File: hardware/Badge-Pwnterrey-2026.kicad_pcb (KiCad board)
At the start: 2 copper layers, 23 parts, among them P1 USB_C_Plug_USB2.0, SW1 RESET, SW2 GPIO, U1 ESP32-C5-WROOM-1-N4, U2 AP2112K-3.3, U3 NT3H2111W0FHK

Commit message: feat(Hw):Init_Floorplan
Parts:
- added SW3: On, Footprints:MSK12C02, F.Cu at (187.8, 82.0)
- moved C1 188.1 mm to (238.4, 65.2), turned to 0 degrees
- moved C3 186.7 mm to (238.4, 66.7), turned to 0 degrees
- moved U1 170.4 mm to (233.2, 78.3), turned to -90 degrees
- moved C4 131.5 mm to (231.9, 58.3)
- moved R1 131.5 mm to (234.8, 58.3)
- moved SW1 131.5 mm to (233.3, 54.5)
- moved F1 124.0 mm to (197.2, 67.1)
- moved R3 124.0 mm to (197.1, 62.6)
- moved R4 124.0 mm to (197.2, 65.6)
- moved P1 124.0 mm to (192.7, 63.9)
- moved R2 101.7 mm to (224.7, 58.4)
- moved C5 101.7 mm to (221.7, 58.4)
- moved SW2 101.7 mm to (223.2, 54.5)
- moved C9 101.0 mm to (199.9, 82.8), turned to 0 degrees
- moved U2 98.3 mm to (199.8, 79.5), turned to 90 degrees
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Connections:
- C9 pad 1: VBUS -> Net-(SW3A-B)
- U2 pad 1: VBUS -> Net-(SW3A-B)
- U2 pad 3: VBUS -> Net-(SW3A-B)
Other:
- board outline added: 54 x 85.6 mm

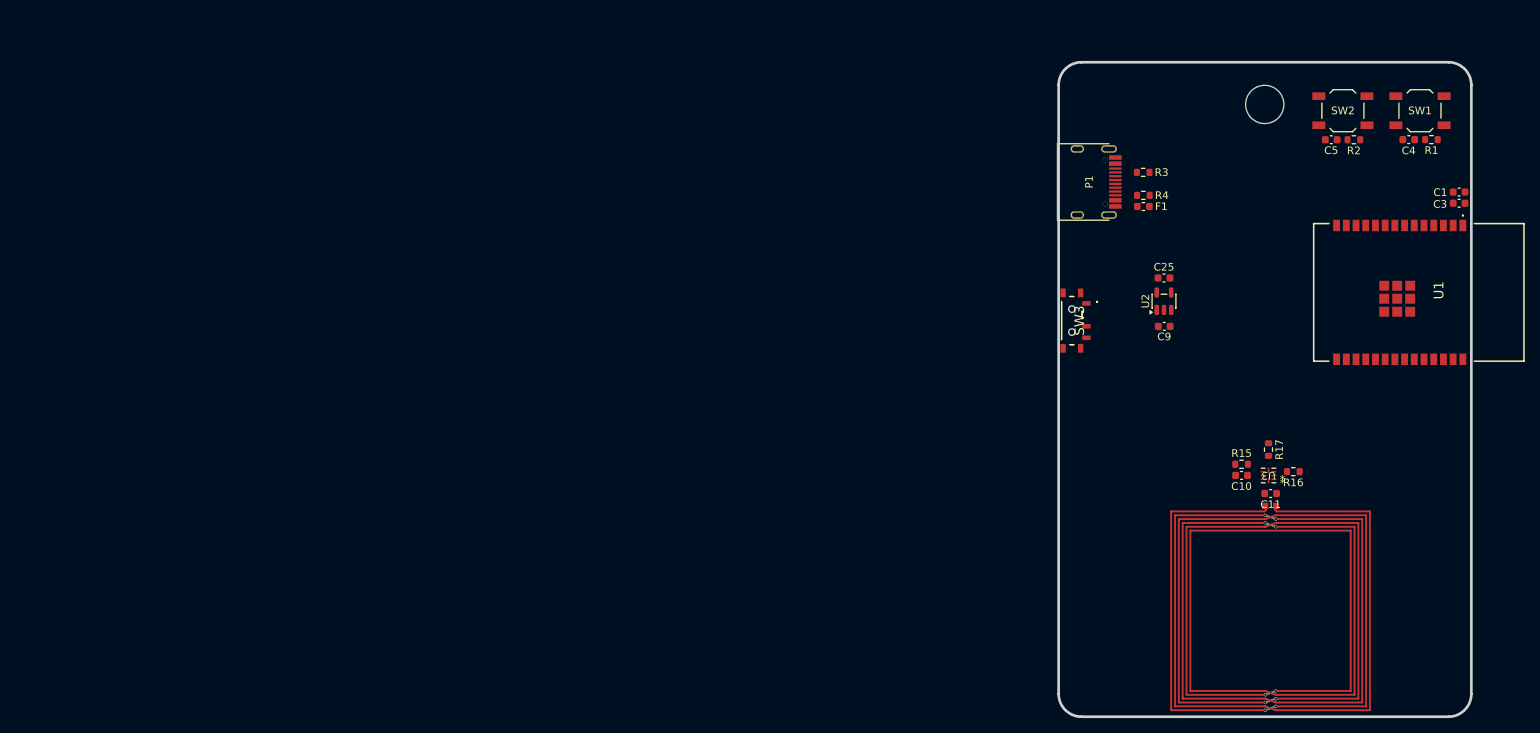
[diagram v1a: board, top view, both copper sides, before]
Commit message: feat(Hw):Update_Schematic_And_Init_Route
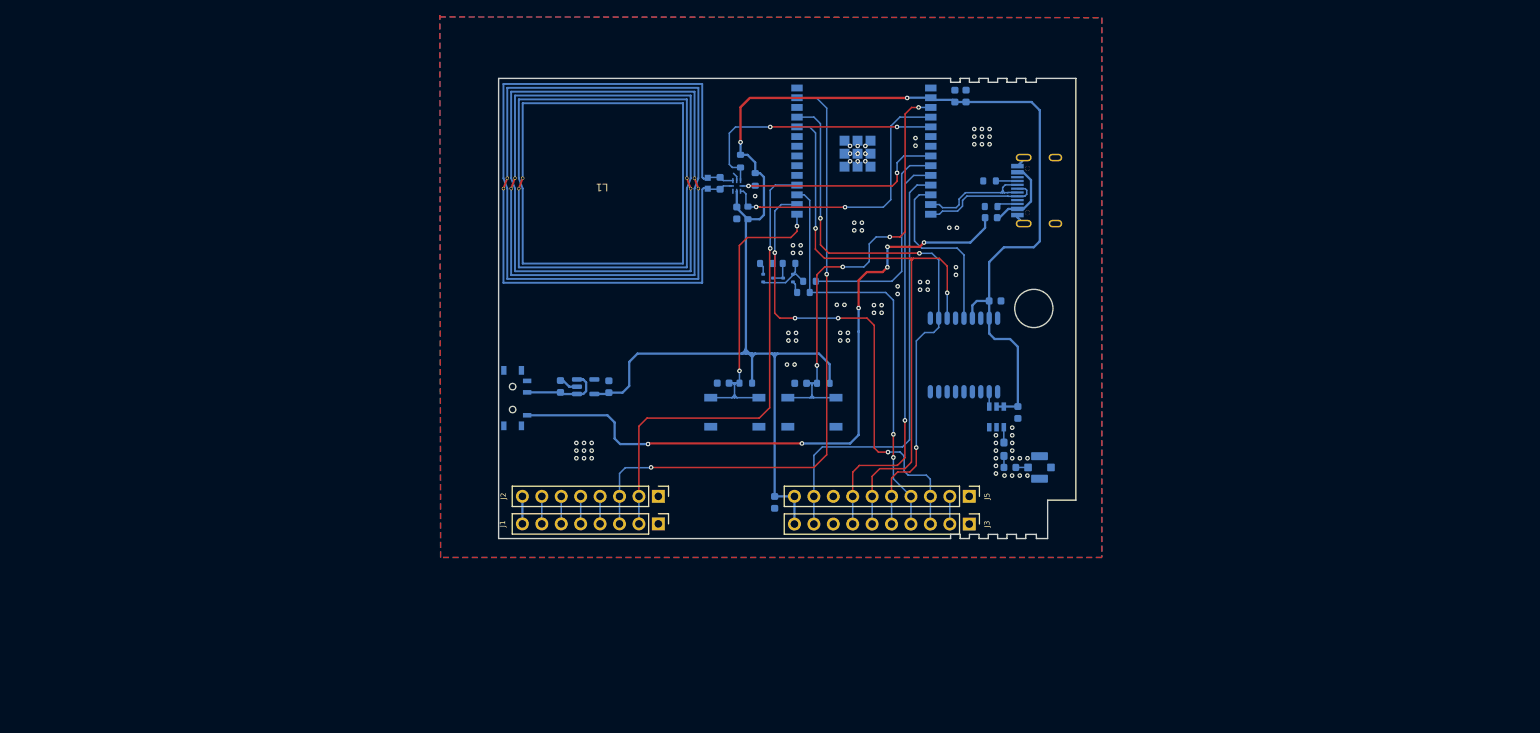
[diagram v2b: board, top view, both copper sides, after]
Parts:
- added AE1: Antenna_Shield, Connector_Coaxial:U.FL_Molex_MCRF_73412-0110_Vertical, B.Cu at (183.6, 101.2)
- added C14: 10uF, Capacitor_SMD:C_0603_1608Metric, B.Cu at (177.8, 79.4)
- added C15: 0.1uF, Capacitor_SMD:C_0603_1608Metric, B.Cu at (180.7, 94.0)
- added C2: 10uF, Capacitor_SMD:C_0603_1608Metric, B.Cu at (148.9, 105.8)
- added C6: 470pF, Capacitor_SMD:C_0603_1608Metric, B.Cu at (179.7, 101.2)
- added J1: Conn_01x08_Socket, Connector_PinHeader_2.54mm:PinHeader_1x08_P2.54mm_Vertical, F.Cu at (133.7, 108.6)
- added J2: Conn_01x08_Socket, Connector_PinHeader_2.54mm:PinHeader_1x08_P2.54mm_Vertical, F.Cu at (133.7, 105.0)
- added J3: Conn_01x10_Socket, Connector_PinHeader_2.54mm:PinHeader_1x10_P2.54mm_Vertical, F.Cu at (174.4, 108.6)
- added J5: Conn_01x10_Socket, Connector_PinHeader_2.54mm:PinHeader_1x10_P2.54mm_Vertical, F.Cu at (174.4, 105.0)
- added L2: 6.8nH, Inductor_SMD:L_0603_1608Metric_Pad1.05x0.95mm_HandSolder, B.Cu at (178.9, 98.8)
- added Q1: DMP2004TK-7, Package_TO_SOT_SMD:SOT-523, B.Cu at (148.1, 76.4)
- added Q2: DMP2004TK-7, Package_TO_SOT_SMD:SOT-523, B.Cu at (150.7, 76.4)
- added R6: 150, Resistor_SMD:R_0603_1608Metric, B.Cu at (153.5, 76.9)
- added R7: 10K, Resistor_SMD:R_0603_1608Metric, B.Cu at (150.8, 74.5)
- added R8: 4k7, Resistor_SMD:R_0603_1608Metric, B.Cu at (147.8, 74.5)
- added R9: 4k7, Resistor_SMD:R_0603_1608Metric, B.Cu at (152.7, 78.3)
- added U4: LNA, Footprints:AT2659S-LSA, B.Cu at (177.9, 94.6)
- added U5: GPS, Footprints:GPSM-SMD_ATGM336H, B.Cu at (173.7, 86.5)
- C1, C10, C11, C25, C3, C4, C5, C9, F1, P1, R1, R15, R16, R17, R2, R3, R4, SW1, SW2, SW3, U1, U2, U3: moved to B.Cu
- L1: moved to F.Cu
- moved L1 103.8 mm to (126.3, 64.1), turned to 180 degrees
- moved SW1 88.8 mm to (153.8, 94.0)
- moved SW2 88.8 mm to (143.7, 94.0)
- moved C4 85.7 mm to (152.3, 90.2)
- moved R1 85.7 mm to (155.3, 90.2)
- moved C5 85.7 mm to (142.2, 90.2)
- moved R2 85.7 mm to (145.2, 90.2)
- moved R16 82.9 mm to (144.5, 61.1), turned to -90 degrees
- moved C11 82.7 mm to (141.8, 64.0), turned to -90 degrees
- moved C9 79.4 mm to (120.9, 90.6), turned to 90 degrees
- moved U3 79.2 mm to (144.0, 64.4), turned to -90 degrees
- moved U2 76.5 mm to (124.2, 90.6), turned to 0 degrees
- moved R17 75.9 mm to (146.4, 63.5)
- moved U1 75.5 mm to (160.6, 57.3), turned to 180 degrees
- moved C10 74.4 mm to (144.0, 67.9), turned to -90 degrees
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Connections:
- C10 pad 1: +3.3V -> +3V3
- R15 pad 1: +3.3V -> +3V3
- R16 pad 1: +3.3V -> +3V3
- R17 pad 1: +3.3V -> +3V3
- U1 pad 10: unconnected-(U1-IO8-Pad10) -> /SWDIO
- U1 pad 11: unconnected-(U1-IO9-Pad11) -> /SWCLK
- U1 pad 12: unconnected-(U1-IO10-Pad12) -> /IO10
- U1 pad 16: unconnected-(U1-IO5-Pad16) -> /LPUART_RX
- U1 pad 17: /FD -> /LPUART_TX
- U1 pad 18: unconnected-(U1-IO27-Pad18) -> /IO27
- U1 pad 24: unconnected-(U1-RX0-Pad24) -> /TX
- U1 pad 25: unconnected-(U1-TX0-Pad25) -> /RX
- U1 pad 27: unconnected-(U1-IO26-Pad27) -> /IO26
- U1 pad 29: (no net) -> GND
- U1 pad 31: unconnected-(U1-ANT2-Pad31) -> GND
- U1 pad 33: (no net) -> GND
- U1 pad 34: (no net) -> GND
- U1 pad 35: (no net) -> GND
- U1 pad 36: (no net) -> GND
- U1 pad 37: (no net) -> GND
- U1 pad 8: unconnected-(U1-IO6-Pad8) -> /FD
- U1 pad 9: unconnected-(U1-IO7-Pad9) -> /SER_PULLUP
- U3 pad 6: +3.3V -> +3V3
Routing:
- net +3V3: track 0.00 -> 205.7 mm, vias 0 -> 2
- net VBUS: track 0.00 -> 89.2 mm, vias 0 -> 6
- net /IO26: track 0.00 -> 84.5 mm, vias 0 -> 2
- net /TX: track 0.00 -> 82.6 mm, vias 0 -> 2
- net /RX: track 0.00 -> 74.3 mm, vias 0 -> 3
- net /LPUART_RX: track 0.00 -> 63.9 mm, vias 0 -> 4
- net /IO27: track 0.00 -> 63.1 mm, vias 0 -> 1
- net /RST: track 0.00 -> 59.4 mm, vias 0 -> 4
- net /SWCLK: track 0.00 -> 57.9 mm
- net /LPUART_TX: track 0.00 -> 55.6 mm, vias 0 -> 2
- net /SWDIO: track 0.00 -> 54.1 mm, vias 0 -> 1
- net /BOOT: track 0.00 -> 39.7 mm, vias 0 -> 2
- net /SDA: track 0.00 -> 37.1 mm, vias 0 -> 2
- net /SCL: track 0.00 -> 34.1 mm, vias 0 -> 2
- net /SER_PULLUP: track 0.00 -> 28.8 mm
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- added copper zone on B.Cu, net GND
- added copper zone on F.Cu, net GND
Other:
- board size 54 x 85.6 mm -> 75.5 x 60.2 mm

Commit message: feat(Hw):Update_Labels
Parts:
- added kibuzzard-6488EEAF: G***, kibuzzard-6488EEAF, B.Cu at (133.7, 101.5)
- added kibuzzard-6488EEAF: G***, kibuzzard-6488EEAF, B.Cu at (174.4, 101.5)
- added kibuzzard-6488EEAF: G***, kibuzzard-6488EEAF, B.Cu at (156.6, 101.5)
- added kibuzzard-6488F75A: G***, kibuzzard-6488F75A, B.Cu at (151.5, 101.5)
- added kibuzzard-648B91CB: G***, kibuzzard-648B91CB, B.Cu at (123.6, 101.5)
- added kibuzzard-648B91E6: G***, kibuzzard-648B91E6, B.Cu at (126.1, 101.5)
- added kibuzzard-648B91FC: G***, kibuzzard-648B91FC, B.Cu at (128.6, 101.5)
- added kibuzzard-648B921B: G***, kibuzzard-648B921B, B.Cu at (131.2, 101.5)
- added kibuzzard-648B922F: G***, kibuzzard-648B922F, B.Cu at (118.5, 101.5)
- added kibuzzard-648B923F: G***, kibuzzard-648B923F, B.Cu at (121.0, 101.5)
- added kibuzzard-648B93B1: G***, kibuzzard-648B93B1, B.Cu at (154.1, 101.5)
- added kibuzzard-648B93BF: G***, kibuzzard-648B93BF, B.Cu at (159.1, 101.5)
- added kibuzzard-648B93D2: G***, kibuzzard-648B93D2, B.Cu at (164.2, 101.5)
- added kibuzzard-648B93E0: G***, kibuzzard-648B93E0, B.Cu at (161.7, 101.5)
- added kibuzzard-648B93EF: G***, kibuzzard-648B93EF, B.Cu at (166.8, 101.5)
- added kibuzzard-648B9401: G***, kibuzzard-648B9401, B.Cu at (169.3, 101.5)
- added kibuzzard-648B9410: G***, kibuzzard-648B9410, B.Cu at (171.8, 101.5)
- added kibuzzard-64E4E5CE: G***, kibuzzard-64E4E5CE, B.Cu at (115.9, 101.5)
